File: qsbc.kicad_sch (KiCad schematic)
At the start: 0 parts

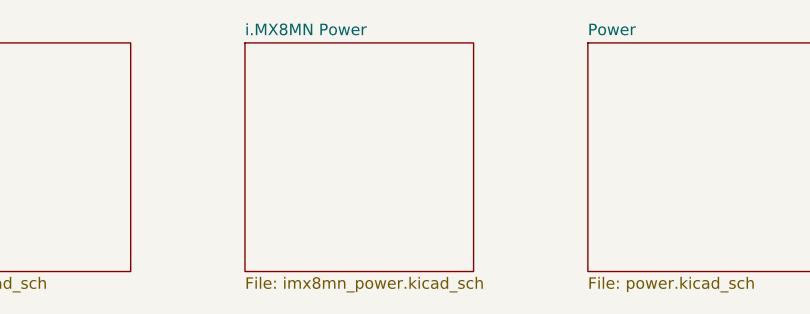
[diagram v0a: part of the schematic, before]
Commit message: move to i.MX8M Mini
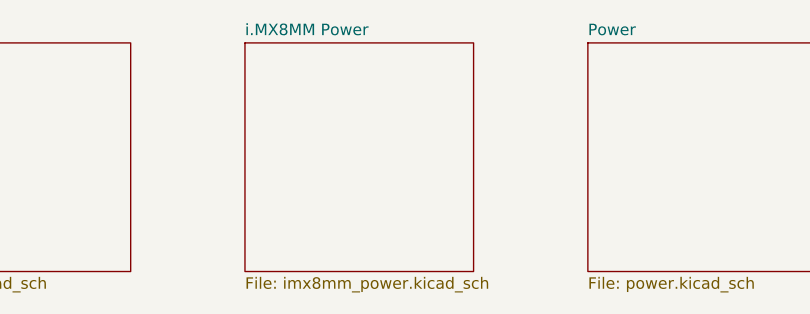
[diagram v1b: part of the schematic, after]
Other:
- sheet i.MX8MN Power renamed i.MX8MM Power
- sheet i.MX8MM Power: file imx8mn_power.kicad_sch -> imx8mm_power.kicad_sch
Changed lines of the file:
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@@
     (stroke (width 0.1524) (type solid) (color 0 0 0 0))
     (fill (color 0 0 0 0.0000))
-    (property "Sheet name" "i.MX8MN Power" (id 0) (at 76.2 37.3884 0)
+    (property "Sheet name" "i.MX8MM Power" (id 0) (at 76.2 37.3884 0)
       (effects (font (size 1.27 1.27)) (justify left bottom))
     )
-    (property "Sheet file" "imx8mn_power.kicad_sch" (id 1) (at 76.2 64.0846 0)
+    (property "Sheet file" "imx8mm_power.kicad_sch" (id 1) (at 76.2 64.0846 0)
       (effects (font (size 1.27 1.27)) (justify left top))
     )
@@
       (reference "R2") (unit 1) (value "240R") (footprint "")
     )
-    (path "/34bccd39-4b2a-4598-80fe-08cfc5b119de/aef83542-6d1d-45bb-ab3e-13f71eacfc03"
-      (reference "U1") (unit 1) (value "MIMX8MN5DVPIZAA") (footprint "qsbc:SOT1967-1")
-    )
-    (path "/ef57cfb9-1220-4106-9f4b-c7611d652afc/6df863b4-4c6d-465e-905c-7867a593c58a"
-      (reference "U1") (unit 2) (value "MIMX8MN5DVPIZAA") (footprint "qsbc:SOT1967-1")
-    )
-    (path "/23aba2cb-1578-4c7b-a15c-a599737ba9cc/0d16079a-0569-48c4-ba9d-c35fb73b6dce"
-      (reference "U1") (unit 3) (value "MIMX8MN5DVPIZAA") (footprint "qsbc:SOT1967-1")
-    )
-    (path "/23aba2cb-1578-4c7b-a15c-a599737ba9cc/19c70350-d4d6-4262-832b-90e8a5038fcb"
-      (reference "U1") (unit 4) (value "MIMX8MN5DVPIZAA") (footprint "qsbc:SOT1967-1")
-    )
-    (path "/996c4a6c-0366-4ef4-ac11-a39cf582fa19/227f7f01-6f5c-4063-b113-964b13a004a4"
-      (reference "U1") (unit 5) (value "MIMX8MN5DVPIZAA") (footprint "qsbc:SOT1967-1")
-    )
-    (path "/23aba2cb-1578-4c7b-a15c-a599737ba9cc/8eb712f6-89f3-4467-b342-df13300d112e"
-      (reference "U1") (unit 6) (value "MIMX8MN5DVPIZAA") (footprint "qsbc:SOT1967-1")
-    )
-    (path "/5d9eebb8-e3be-4676-9eb3-56276e862bd5/2ced1d1d-5d1f-412e-9b29-12cfa573e48d"
-      (reference "U1") (unit 7) (value "MIMX8MN5DVPIZAA") (footprint "qsbc:SOT1967-1")
-    )
-    (path "/84b83f54-5bc0-485b-85b5-5fe5cb64a272/627530eb-9df8-4cf6-8020-d1687b8615b4"
-      (reference "U1") (unit 8) (value "MIMX8MN5DVPIZAA") (footprint "qsbc:SOT1967-1")
-    )
-    (path "/84b83f54-5bc0-485b-85b5-5fe5cb64a272/d7fcd768-4871-4b9e-a504-07c4de13b453"
-      (reference "U1") (unit 9) (value "MIMX8MN5DVPIZAA") (footprint "qsbc:SOT1967-1")
-    )
-    (path "/996c4a6c-0366-4ef4-ac11-a39cf582fa19/6cac47cc-6493-417f-a799-83bbf044b0b6"
-      (reference "U1") (unit 10) (value "MIMX8MN5DVPIZAA") (footprint "qsbc:SOT1967-1")
-    )
-    (path "/996c4a6c-0366-4ef4-ac11-a39cf582fa19/2c3c5f0e-50e5-4fa3-9403-52fdc2031026"
-      (reference "U1") (unit 11) (value "MIMX8MN5DVPIZAA") (footprint "qsbc:SOT1967-1")
-    )
-    (path "/35af9dad-35b7-42c4-b835-c17a87e64e5a/466e78a7-b203-41b7-8cdd-1bf4f8d2e39f"
-      (reference "U1") (unit 12) (value "MIMX8MN5DVPIZAA") (footprint "qsbc:SOT1967-1")
-    )
-    (path "/23aba2cb-1578-4c7b-a15c-a599737ba9cc/bc2217f9-dff0-485b-bae6-3c6c0b3bd89c"
-      (reference "U1") (unit 13) (value "MIMX8MN5DVPIZAA") (footprint "qsbc:SOT1967-1")
-    )
-    (path "/23aba2cb-1578-4c7b-a15c-a599737ba9cc/cbab4776-9b36-4bba-b748-7d2d24a17e22"
-      (reference "U1") (unit 14) (value "MIMX8MN5DVPIZAA") (footprint "qsbc:SOT1967-1")
-    )
-    (path "/23aba2cb-1578-4c7b-a15c-a599737ba9cc/239f4d6c-0c09-4614-820a-347cbcdce6c8"
-      (reference "U1") (unit 15) (value "MIMX8MN5DVPIZAA") (footprint "qsbc:SOT1967-1")
-    )
     (path "/ef57cfb9-1220-4106-9f4b-c7611d652afc/cddf9ec2-bc4e-457d-b1a2-16c4be6862d5"
       (reference "U3") (unit 1) (value "MT40A1G16KD-062E") (footprint "qsbc:MICRON-FBGA-96")
     )
+    (path "/34bccd39-4b2a-4598-80fe-08cfc5b119de/2cda1c19-f48e-4aab-b64b-652849aa66cf"
+      (reference "U?") (unit 1) (value "MIMX8MM6DVTLZAA") (footprint "qsbc:SOT1967-1")
+    )
+    (path "/ef57cfb9-1220-4106-9f4b-c7611d652afc/129d791b-f44a-41cb-b00f-75c71aabf700"
+      (reference "U?") (unit 2) (value "MIMX8MM6DVTLZAA") (footprint "qsbc:SOT1967-1")
+    )
+    (path "/23aba2cb-1578-4c7b-a15c-a599737ba9cc/3dab74a9-7c4c-4ce5-96f7-fb27ab8663bc"
+      (reference "U?") (unit 3) (value "MIMX8MM6DVTLZAA") (footprint "qsbc:SOT1967-1")
+    )
+    (path "/23aba2cb-1578-4c7b-a15c-a599737ba9cc/1e92341d-a800-4e2b-9de7-c0d97c33455e"
+      (reference "U?") (unit 4) (value "MIMX8MM6DVTLZAA") (footprint "qsbc:SOT1967-1")
+    )
+    (path "/996c4a6c-0366-4ef4-ac11-a39cf582fa19/94ee666d-f2f0-4731-85f4-2c7083a560b6"
+      (reference "U?") (unit 5) (value "MIMX8MM6DVTLZAA") (footprint "qsbc:SOT1967-1")
+    )
+    (path "/23aba2cb-1578-4c7b-a15c-a599737ba9cc/04ffe837-6900-4c13-8040-79fbc71e6466"
+      (reference "U?") (unit 6) (value "MIMX8MM6DVTLZAA") (footprint "qsbc:SOT1967-1")
+    )
+    (path "/5d9eebb8-e3be-4676-9eb3-56276e862bd5/3ff70096-72c2-4bbd-9af0-0b28f064dc5e"
+      (reference "U?") (unit 7) (value "MIMX8MM6DVTLZAA") (footprint "qsbc:SOT1967-1")
+    )
+    (path "/84b83f54-5bc0-485b-85b5-5fe5cb64a272/32768a81-c87c-4492-8fd3-282fb9403d28"
+      (reference "U?") (unit 8) (value "MIMX8MM6DVTLZAA") (footprint "qsbc:SOT1967-1")
+    )
+    (path "/84b83f54-5bc0-485b-85b5-5fe5cb64a272/f32a06e0-a001-4b31-8d54-57f241f1d875"
+      (reference "U?") (unit 9) (value "MIMX8MM6DVTLZAA") (footprint "qsbc:SOT1967-1")
+    )
+    (path "/996c4a6c-0366-4ef4-ac11-a39cf582fa19/324c8de4-e8af-44db-aa97-2b056749636a"
+      (reference "U?") (unit 10) (value "MIMX8MM6DVTLZAA") (footprint "qsbc:SOT1967-1")
+    )
+    (path "/996c4a6c-0366-4ef4-ac11-a39cf582fa19/a291cd00-bdf4-4061-8893-1d0cd92fd0f6"
+      (reference "U?") (unit 11) (value "MIMX8MM6DVTLZAA") (footprint "qsbc:SOT1967-1")
+    )
+    (path "/35af9dad-35b7-42c4-b835-c17a87e64e5a/d7d59d35-ec2b-46c0-a6b3-7c0fa1e395be"
+      (reference "U?") (unit 12) (value "MIMX8MM6DVTLZAA") (footprint "qsbc:SOT1967-1")
+    )
+    (path "/23aba2cb-1578-4c7b-a15c-a599737ba9cc/10e6fbb9-cd5b-4d25-a871-b5d636bc3f0e"
+      (reference "U?") (unit 13) (value "MIMX8MM6DVTLZAA") (footprint "qsbc:SOT1967-1")
+    )
+    (path "/23aba2cb-1578-4c7b-a15c-a599737ba9cc/8ef2f740-1703-4c34-988d-091a934f446f"
+      (reference "U?") (unit 14) (value "MIMX8MM6DVTLZAA") (footprint "qsbc:SOT1967-1")
+    )
+    (path "/23aba2cb-1578-4c7b-a15c-a599737ba9cc/1dafccc9-9fb1-4fd7-8e91-ea957942416e"
+      (reference "U?") (unit 15) (value "MIMX8MM6DVTLZAA") (footprint "qsbc:SOT1967-1")
+    )
+    (path "/23aba2cb-1578-4c7b-a15c-a599737ba9cc/180bf6bc-0585-45d8-b29b-ea86cd51264d"
+      (reference "U?") (unit 16) (value "MIMX8MM6DVTLZAA") (footprint "qsbc:SOT1967-1")
+    )
+    (path "/23aba2cb-1578-4c7b-a15c-a599737ba9cc/c8c2e3d6-e64f-4f7d-9cbc-e2cbb0e42fc6"
+      (reference "U?") (unit 17) (value "MIMX8MM6DVTLZAA") (footprint "qsbc:SOT1967-1")
+    )
   )

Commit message: misc work, usb sch done
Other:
- added sheet PCIe (pcie.kicad_sch)
- added sheet UART (uart.kicad_sch)
- sheet Power ports: added NVCC_DRAM_1.2V, NVCC_SD2, NVCC_SNVS_1P8, VDDA_1.8V, VDD_1.8V, VDD_3.3V, VDD_ARM_0.9V, VDD_DRAM_xPU_0.9V, VDD_PHY_0.9V, VDD_PHY_1.2V, VDD_SNVS_0.8V, VDD_SOC_0.8V, VPP_2.5V, VSYS_5V; removed none
- sheet USB ports: added I2Cx_SCL, I2Cx_SDA, UART2_CTS, UART2_RTS, UART2_RXI, UART2_TXO, USB1_VBUS_EN, USB2_VBUS_EN, VDD_1.8V, VDD_3.3V, VSYS_5V, ~{USB1_INT}, ~{USB1_VBUS_FLT}, ~{USB2_INT}, ~{USB2_VBUS_FLT}; removed none

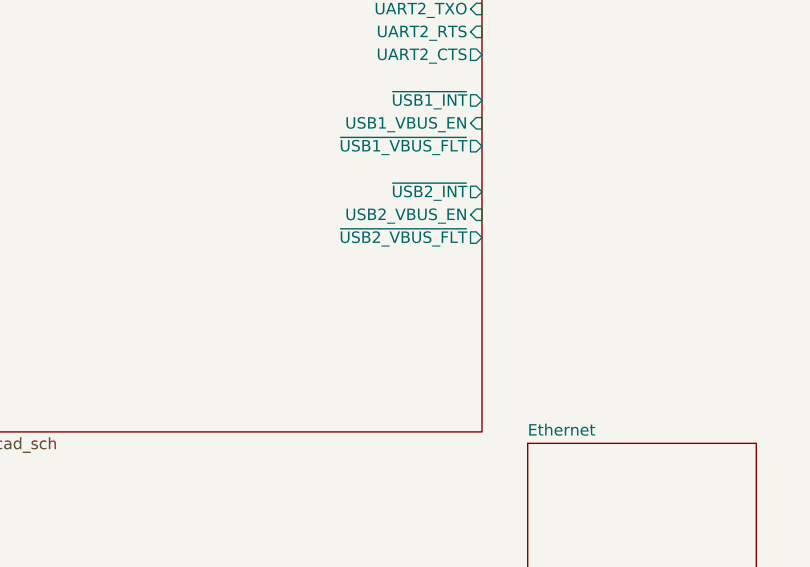
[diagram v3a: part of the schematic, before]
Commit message: enet sch done, other misc sch work
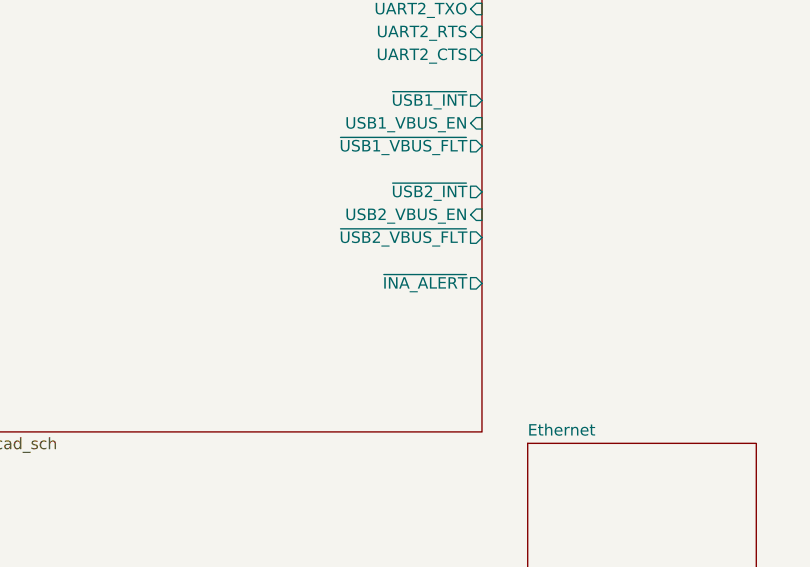
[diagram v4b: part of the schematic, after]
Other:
- sheet USB ports: added ~{INA_ALERT}; removed none

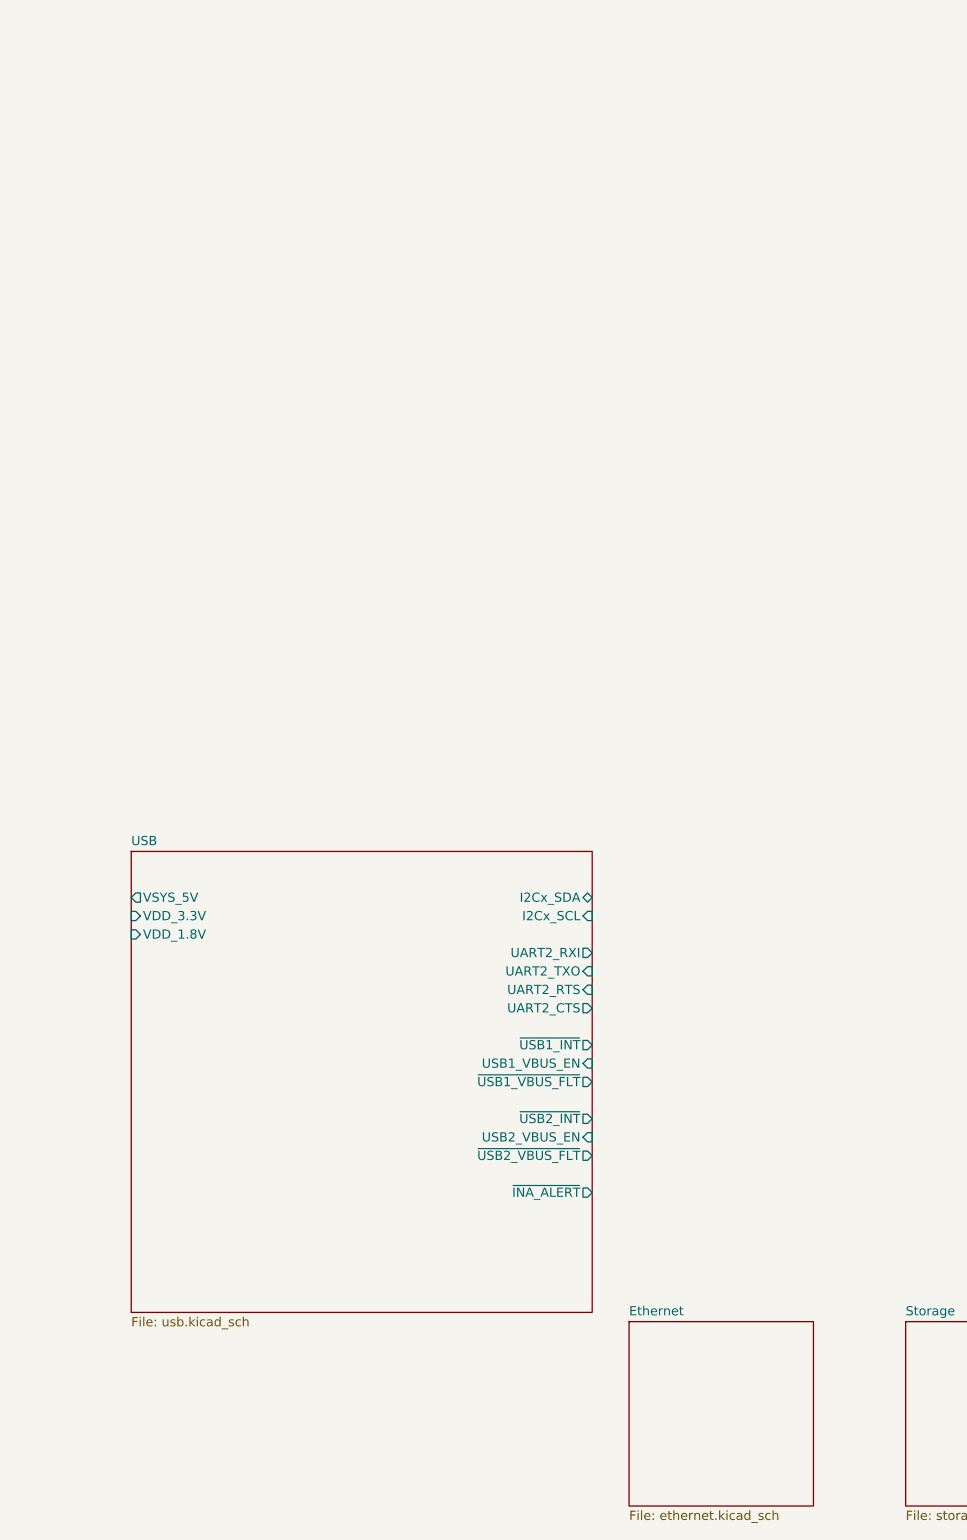
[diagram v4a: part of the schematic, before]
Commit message: enet: add hierarchial labels
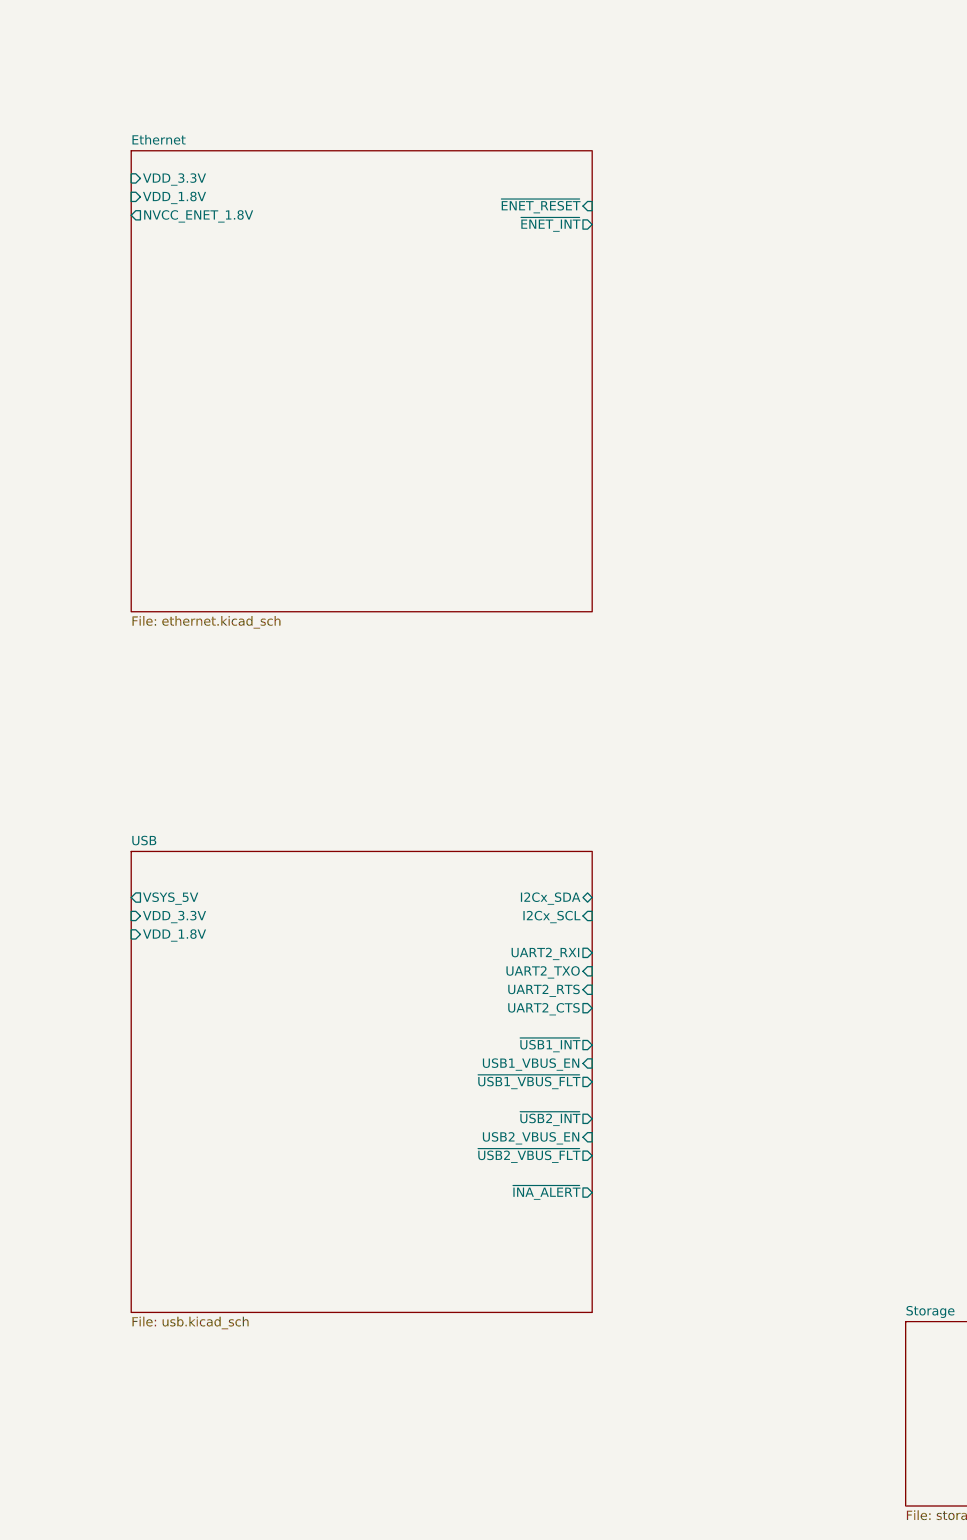
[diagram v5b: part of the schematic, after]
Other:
- sheet Ethernet ports: added NVCC_ENET_1.8V, VDD_1.8V, VDD_3.3V, ~{ENET_INT}, ~{ENET_RESET}; removed none
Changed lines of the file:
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@@
     )
   )
-  (sheet (at 208.28 351.79) (size 25.4 25.4) (fields_autoplaced)
+  (sheet (at 139.7 190.5) (size 63.5 63.5) (fields_autoplaced)
     (stroke (width 0.1524) (type solid) (color 0 0 0 0))
     (fill (color 0 0 0 0.0000))
-    (property "Sheet name" "Ethernet" (id 0) (at 208.28 351.0784 0)
+    (property "Sheet name" "Ethernet" (id 0) (at 139.7 189.7884 0)
       (effects (font (size 1.27 1.27)) (justify left bottom))
     )
-    (property "Sheet file" "ethernet.kicad_sch" (id 1) (at 208.28 377.7746 0)
+    (property "Sheet file" "ethernet.kicad_sch" (id 1) (at 139.7 254.5846 0)
       (effects (font (size 1.27 1.27)) (justify left top))
     )
+    (pin "VDD_1.8V" input (at 139.7 196.85 180)
+      (effects (font (size 1.27 1.27)) (justify left))
+    )
+    (pin "VDD_3.3V" input (at 139.7 194.31 180)
+      (effects (font (size 1.27 1.27)) (justify left))
+    )
+    (pin "~{ENET_RESET}" input (at 203.2 198.12 0)
+      (effects (font (size 1.27 1.27)) (justify right))
+    )
+    (pin "NVCC_ENET_1.8V" output (at 139.7 199.39 180)
+      (effects (font (size 1.27 1.27)) (justify left))
+    )
+    (pin "~{ENET_INT}" output (at 203.2 200.66 0)
+      (effects (font (size 1.27 1.27)) (justify right))
+    )
   )

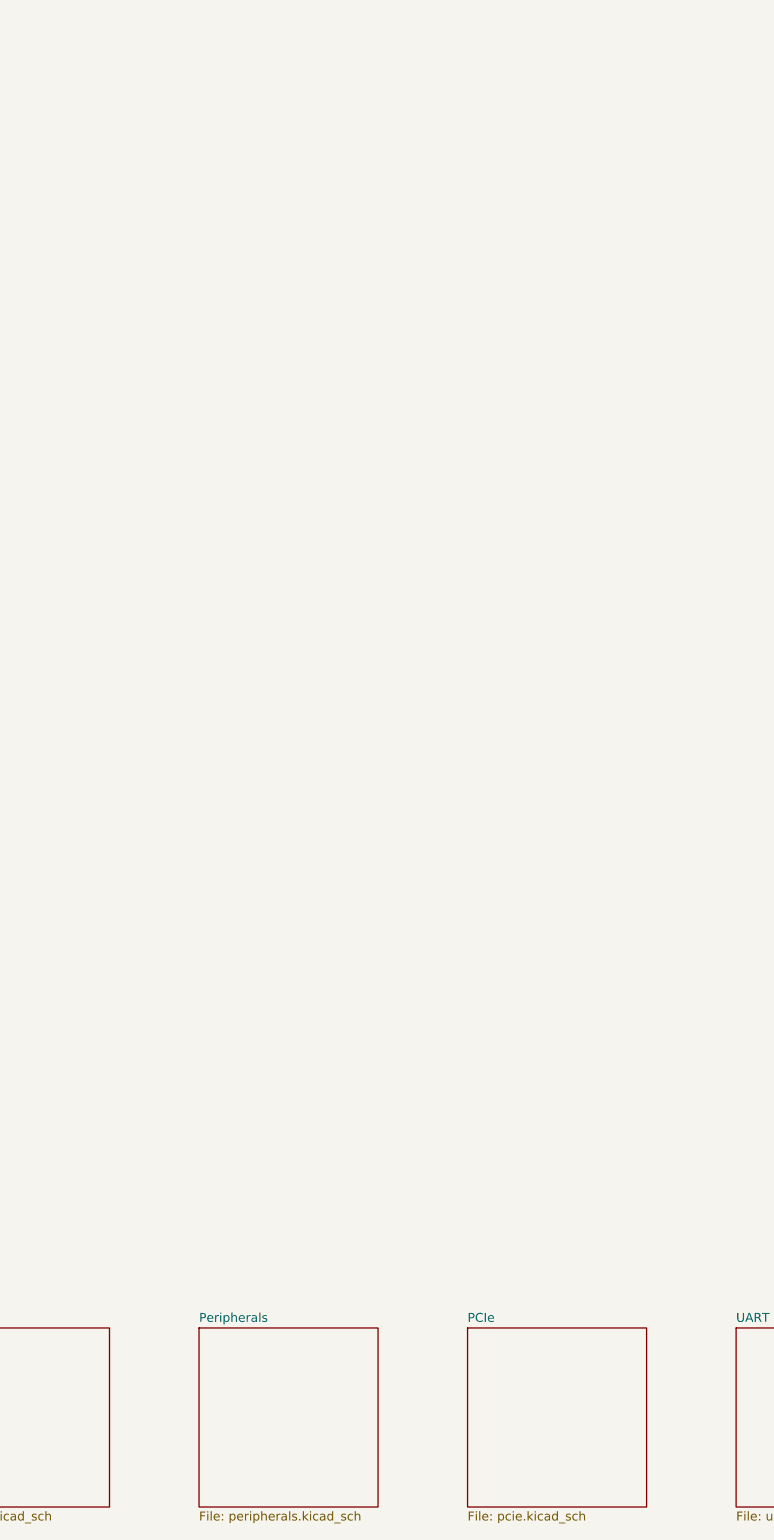
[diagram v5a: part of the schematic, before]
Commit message: pcie done, misc fixes for usb, enet
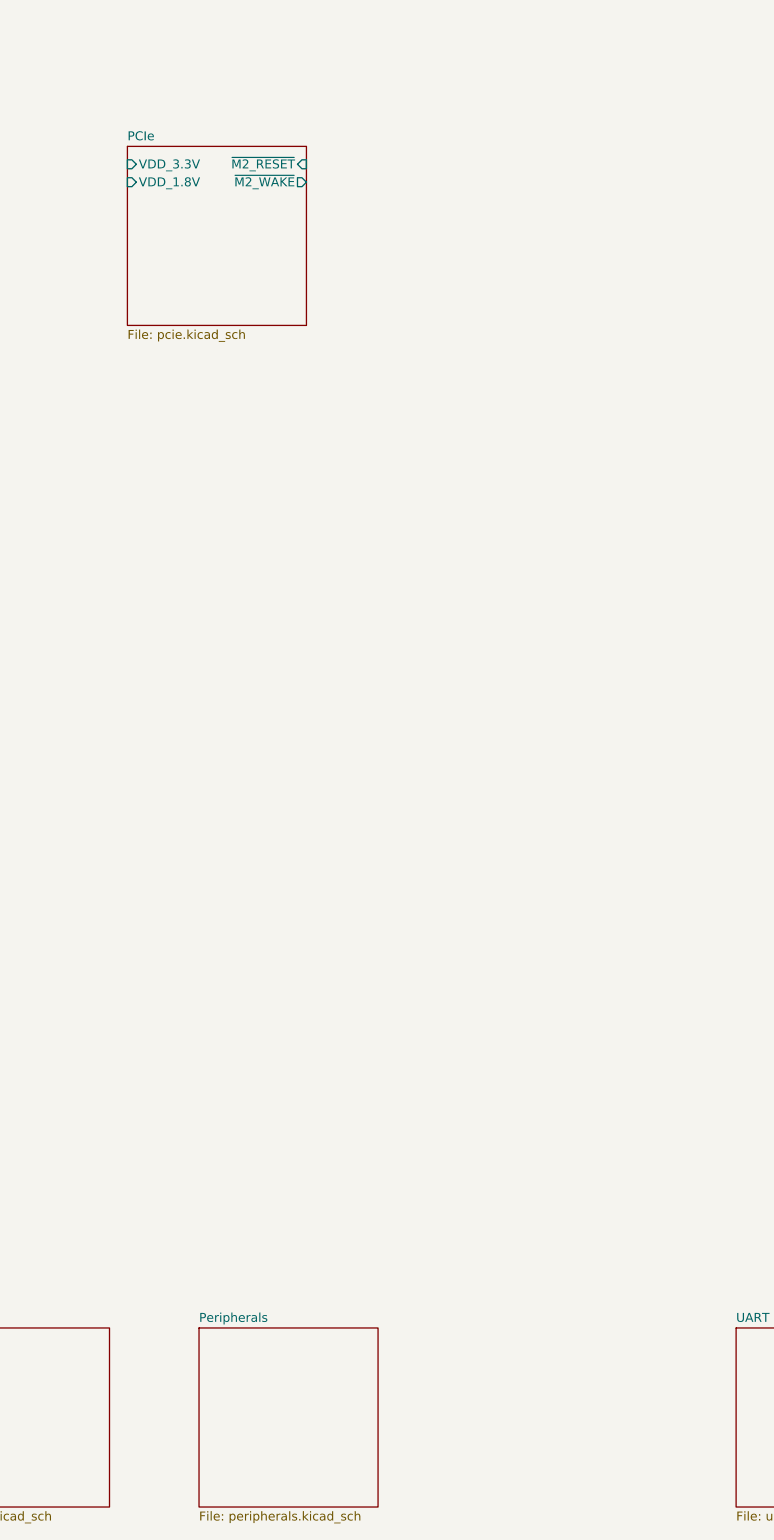
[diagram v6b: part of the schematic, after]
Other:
- sheet PCIe ports: added VDD_1.8V, VDD_3.3V, ~{M2_RESET}, ~{M2_WAKE}; removed none
